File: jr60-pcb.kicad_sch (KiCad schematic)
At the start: 21 parts

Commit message: started matrix
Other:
- added sheet Matrix (matrix.kicad_sch)
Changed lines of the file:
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@@
     (pin "1")
+  )
+  (sheet (at 190.5 137.16) (size 12.7 3.81) (fields_autoplaced)
+    (stroke (width 0.1524) (type solid) (color 0 0 0 0))
+    (fill (color 0 0 0 0.0000))
+    (property "Sheet name" "Matrix" (id 0) (at 190.5 136.4484 0)
+      (effects (font (size 1.27 1.27)) (justify left bottom))
+    )
+    (property "Sheet file" "matrix.kicad_sch" (id 1) (at 190.5 141.5546 0)
+      (effects (font (size 1.27 1.27)) (justify left top))
+    )
   )
   (sheet_instances
     (path "/" (page "1"))
+    (path "/a32c9d6a-15a8-4264-8189-26275dcc1052" (page "2"))
   )
   (symbol_instances
@@
       (reference "C?") (unit 1) (value "22pF") (footprint "")
     )
+    (path "/a32c9d6a-15a8-4264-8189-26275dcc1052/00a164fa-38f9-42b5-9176-f808ef7fc89b"
+      (reference "D?") (unit 1) (value "D") (footprint "")
+    )
+    (path "/a32c9d6a-15a8-4264-8189-26275dcc1052/1690ef0f-ed90-4e63-8703-bcf22794eefd"
+      (reference "D?") (unit 1) (value "D") (footprint "")
+    )
+    (path "/a32c9d6a-15a8-4264-8189-26275dcc1052/2055ae58-06be-409a-ba1d-226477b90fa3"
+      (reference "D?") (unit 1) (value "D") (footprint "")
+    )
+    (path "/a32c9d6a-15a8-4264-8189-26275dcc1052/256b5fc0-1704-4c45-8ea4-4429ee40f749"
+      (reference "D?") (unit 1) (value "D") (footprint "")
+    )
+    (path "/a32c9d6a-15a8-4264-8189-26275dcc1052/2daa499a-0452-4e25-a168-f52ca4e61051"
+      (reference "D?") (unit 1) (value "D") (footprint "")
+    )
+    (path "/a32c9d6a-15a8-4264-8189-26275dcc1052/4475a45f-f66b-4d46-a6b3-5d0b7a07f381"
+      (reference "D?") (unit 1) (value "D") (footprint "")
+    )
+    (path "/a32c9d6a-15a8-4264-8189-26275dcc1052/673fbb2d-67e6-4422-babd-1c722f27fe06"
+      (reference "D?") (unit 1) (value "D") (footprint "")
+    )
+    (path "/a32c9d6a-15a8-4264-8189-26275dcc1052/6aa7918a-25ec-4234-ab4e-f36b24d3656e"
+      (reference "D?") (unit 1) (value "D") (footprint "")
+    )
+    (path "/a32c9d6a-15a8-4264-8189-26275dcc1052/6fa366ad-4923-4d19-8802-676ddee5e0e0"
+      (reference "D?") (unit 1) (value "D") (footprint "")
+    )
+    (path "/a32c9d6a-15a8-4264-8189-26275dcc1052/c1094195-1728-48eb-8a50-fb01f7df6b81"
+      (reference "D?") (unit 1) (value "D") (footprint "")
+    )
+    (path "/a32c9d6a-15a8-4264-8189-26275dcc1052/daefa49c-c704-4635-9fa9-c4869461e1d4"
+      (reference "D?") (unit 1) (value "D") (footprint "")
+    )
+    (path "/a32c9d6a-15a8-4264-8189-26275dcc1052/e3ffa089-507a-4b9c-8ba1-bd98d2fa1ee4"
+      (reference "D?") (unit 1) (value "D") (footprint "")
+    )
+    (path "/a32c9d6a-15a8-4264-8189-26275dcc1052/f284845e-8cec-4b95-9641-34a7256df181"
+      (reference "D?") (unit 1) (value "D") (footprint "")
+    )
+    (path "/a32c9d6a-15a8-4264-8189-26275dcc1052/f9cbd109-bc43-4c58-8da7-c90cf3420d21"
+      (reference "D?") (unit 1) (value "D") (footprint "")
+    )
     (path "/c0d774bc-a44d-4b6a-9b9c-a6a7c3bfec6e"
       (reference "F?") (unit 1) (value "Polyfuse_Small") (footprint "")
@@
       (reference "J?") (unit 1) (value "AVR-ISP-6") (footprint "")
     )
+    (path "/a32c9d6a-15a8-4264-8189-26275dcc1052/1a1701f0-a37f-44d1-8366-4f1edb2b9779"
+      (reference "K?") (unit 1) (value "SW_Push") (footprint "")
+    )
+    (path "/a32c9d6a-15a8-4264-8189-26275dcc1052/218fdd50-8063-47dd-869e-3c66a52712ca"
+      (reference "K?") (unit 1) (value "SW_Push") (footprint "")
+    )
+    (path "/a32c9d6a-15a8-4264-8189-26275dcc1052/2a6cf2fc-09a9-4db6-82ab-be40098129f8"
+      (reference "K?") (unit 1) (value "SW_Push") (footprint "")
+    )
+    (path "/a32c9d6a-15a8-4264-8189-26275dcc1052/497bc920-a0c1-4136-9bcf-893071f951d9"
+      (reference "K?") (unit 1) (value "SW_Push") (footprint "")
+    )
+    (path "/a32c9d6a-15a8-4264-8189-26275dcc1052/68e190f2-d860-4fdd-b61c-0f7741ce89fc"
+      (reference "K?") (unit 1) (value "SW_Push") (footprint "")
+    )
+    (path "/a32c9d6a-15a8-4264-8189-26275dcc1052/79d9e2c5-69c7-4b71-8e1a-5d45705f6af0"
+      (reference "K?") (unit 1) (value "SW_Push") (footprint "")
+    )
+    (path "/a32c9d6a-15a8-4264-8189-26275dcc1052/917338b5-ee95-47c0-8555-7931f20dad58"
+      (reference "K?") (unit 1) (value "SW_Push") (footprint "")
+    )
+    (path "/a32c9d6a-15a8-4264-8189-26275dcc1052/9302bd53-ef05-46bf-8ffa-7afdd80f9350"
+      (reference "K?") (unit 1) (value "SW_Push") (footprint "")
+    )
+    (path "/a32c9d6a-15a8-4264-8189-26275dcc1052/acd53b94-623c-43fd-8dc1-2293fa782ed0"
+      (reference "K?") (unit 1) (value "SW_Push") (footprint "")
+    )
+    (path "/a32c9d6a-15a8-4264-8189-26275dcc1052/baf2d5a9-c7ab-476c-b992-2d32105450ab"
+      (reference "K?") (unit 1) (value "SW_Push") (footprint "")
+    )
+    (path "/a32c9d6a-15a8-4264-8189-26275dcc1052/bc588dd7-6cd7-4f4f-bfeb-3b9f971a05ce"
+      (reference "K?") (unit 1) (value "SW_Push") (footprint "")
+    )
+    (path "/a32c9d6a-15a8-4264-8189-26275dcc1052/bfaabf9f-8945-4329-9578-c89d395de672"
+      (reference "K?") (unit 1) (value "SW_Push") (footprint "")
+    )
+    (path "/a32c9d6a-15a8-4264-8189-26275dcc1052/c64f3bde-769f-46f9-900b-e94fb5716cdc"
+      (reference "K?") (unit 1) (value "SW_Push") (footprint "")
+    )
+    (path "/a32c9d6a-15a8-4264-8189-26275dcc1052/d4076c6d-89b3-4ef4-aebf-2b683fcda264"
+      (reference "K?") (unit 1) (value "SW_Push") (footprint "")
+    )
     (path "/0b615a32-9f1a-432f-9d20-2774406301bf"

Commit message: finished schematic
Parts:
- gave numbers to parts that had none: 21
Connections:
- net row0: now reaches U1.1 (PE6)
- net col8: now reaches U1.19 (PD1)
- net col9: now reaches U1.20 (PD2)
- net col10: now reaches U1.21 (PD3)
- net col11: now reaches U1.22 (PD5)
- net col12: now reaches U1.25 (PD4)
- net col13: now reaches U1.26 (PD6)
- net col0: now reaches U1.28 (PB4)
- net col1: now reaches U1.29 (PB5)
- net col2: now reaches U1.30 (PB6)
- net col3: now reaches U1.31 (PC6)
- net col4: now reaches U1.32 (PC7)
- net col6: now reaches U1.36 (PF7)
- net col5: now reaches U1.37 (PF6)
- net row1: now reaches U1.38 (PF5)
- net row4: now reaches U1.39 (PF4)
- net row3: now reaches U1.40 (PF1)
- net row2: now reaches U1.41 (PF0)
- net col7: now reaches U1.8 (PB0)
- no-connect marks 3 -> 6

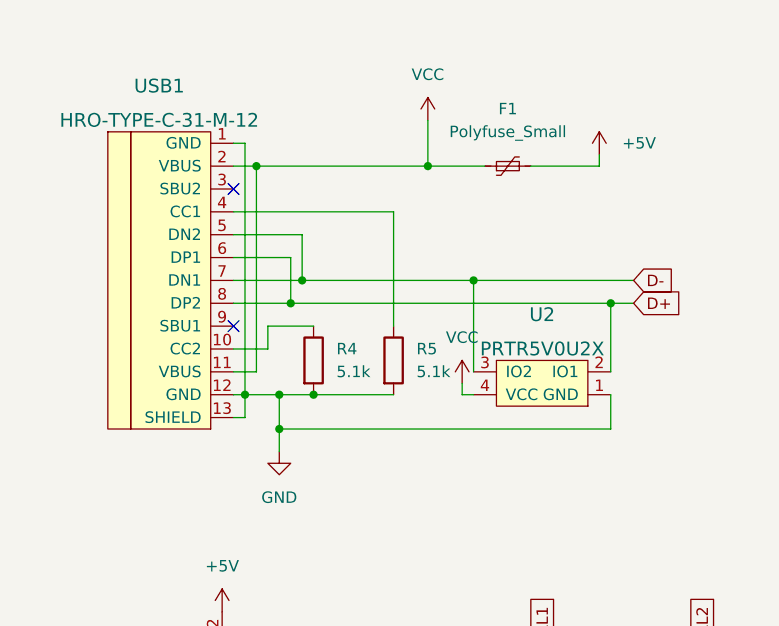
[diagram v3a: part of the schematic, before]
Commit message: added power flags
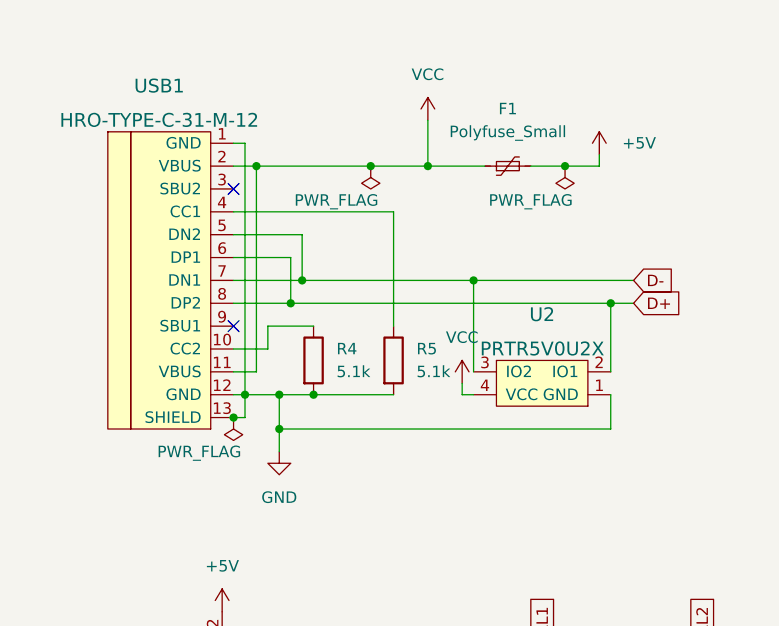
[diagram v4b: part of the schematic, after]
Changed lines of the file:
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@@
   (junction (at 195.58 49.53) (diameter 0) (color 0 0 0 0)
   )
+  (junction (at 128.27 82.55) (diameter 0) (color 0 0 0 0)
+  )
   (junction (at 129.54 53.34) (diameter 0) (color 0 0 0 0)
   )
@@
   (junction (at 175.26 49.53) (diameter 0) (color 0 0 0 0)
   )
+  (junction (at 113.03 110.49) (diameter 0) (color 0 0 0 0)
+  )
   (junction (at 185.42 54.61) (diameter 0) (color 0 0 0 0)
+  )
+  (junction (at 149.86 82.55) (diameter 0) (color 0 0 0 0)
   )
   (junction (at 195.58 54.61) (diameter 0) (color 0 0 0 0)
@@
     (stroke (width 0) (type default) (color 0 0 0 0))
   )
+  (wire (pts (xy 128.27 82.55) (xy 134.62 82.55))
+    (stroke (width 0) (type default) (color 0 0 0 0))
+  )
   (wire (pts (xy 269.24 69.85) (xy 255.27 69.85))
     (stroke (width 0) (type default) (color 0 0 0 0))
@@
     (stroke (width 0) (type default) (color 0 0 0 0))
   )
+  (wire (pts (xy 149.86 82.55) (xy 146.05 82.55))
+    (stroke (width 0) (type default) (color 0 0 0 0))
+  )
   (wire (pts (xy 156.21 151.13) (xy 161.29 151.13))
     (stroke (width 0) (type default) (color 0 0 0 0))
@@
     (stroke (width 0) (type default) (color 0 0 0 0))
   )
-  (wire (pts (xy 153.67 82.55) (xy 146.05 82.55))
+  (wire (pts (xy 153.67 82.55) (xy 149.86 82.55))
     (stroke (width 0) (type default) (color 0 0 0 0))
   )
@@
     (stroke (width 0) (type default) (color 0 0 0 0))
   )
-  (wire (pts (xy 115.57 82.55) (xy 134.62 82.55))
+  (wire (pts (xy 115.57 82.55) (xy 128.27 82.55))
     (stroke (width 0) (type default) (color 0 0 0 0))
   )
@@
     (pin "2")
   )
+  (symbol (lib_id "power:PWR_FLAG") (at 149.86 82.55 0) (mirror x) (unit 1)
+    (in_bom yes) (on_board yes)
+    (property "Reference" "#FLG0102" (id 0) (at 149.86 84.455 0)
+      (effects (font (size 1.27 1.27)) hide)
+    )
+    (property "Value" "PWR_FLAG" (id 1) (at 146.05 86.36 0))
+    (property "Footprint" "" (id 2) (at 149.86 82.55 0)
+      (effects (font (size 1.27 1.27)) hide)
+    )
+    (property "Datasheet" "~" (id 3) (at 149.86 82.55 0)
+      (effects (font (size 1.27 1.27)) hide)
+    )
+    (pin "1")
+  )
   (symbol (lib_id "power:+5V") (at 129.54 39.37 0) (unit 1)
     (in_bom yes) (on_board yes) (fields_autoplaced)
@@
     )
     (property "Datasheet" "" (id 3) (at 185.42 58.42 0)
+      (effects (font (size 1.27 1.27)) hide)
+    )
+    (pin "1")
+  )
+  (symbol (lib_id "power:PWR_FLAG") (at 128.27 82.55 0) (mirror x) (unit 1)
+    (in_bom yes) (on_board yes)
+    (property "Reference" "#FLG0101" (id 0) (at 128.27 84.455 0)
+      (effects (font (size 1.27 1.27)) hide)
+    )
+    (property "Value" "PWR_FLAG" (id 1) (at 124.46 86.36 0))
+    (property "Footprint" "" (id 2) (at 128.27 82.55 0)
+      (effects (font (size 1.27 1.27)) hide)
+    )
+    (property "Datasheet" "~" (id 3) (at 128.27 82.55 0)
       (effects (font (size 1.27 1.27)) hide)
     )
@@
     )
     (property "Datasheet" "" (id 3) (at 138.43 106.68 0)
+      (effects (font (size 1.27 1.27)) hide)
+    )
+    (pin "1")
+  )
+  (symbol (lib_id "power:PWR_FLAG") (at 113.03 110.49 0) (mirror x) (unit 1)
+    (in_bom yes) (on_board yes)
+    (property "Reference" "#FLG0103" (id 0) (at 113.03 112.395 0)
+      (effects (font (size 1.27 1.27)) hide)
+    )
+    (property "Value" "PWR_FLAG" (id 1) (at 109.22 114.3 0))
+    (property "Footprint" "" (id 2) (at 113.03 110.49 0)
+      (effects (font (size 1.27 1.27)) hide)
+    )
+    (property "Datasheet" "~" (id 3) (at 113.03 110.49 0)
       (effects (font (size 1.27 1.27)) hide)
     )
@@
   )
   (symbol_instances
+    (path "/5519e27d-ed94-4fc9-8e77-8f0d1e02ee3d"
+      (reference "#FLG0101") (unit 1) (value "PWR_FLAG") (footprint "")
+    )
+    (path "/0cfec389-6b73-4526-b5a9-72df05e052d3"
+      (reference "#FLG0102") (unit 1) (value "PWR_FLAG") (footprint "")
+    )
+    (path "/e3c81438-fb8d-4106-9e8f-d710c372b033"
+      (reference "#FLG0103") (unit 1) (value "PWR_FLAG") (footprint "")
+    )
     (path "/16adff72-6aad-4163-9f91-24e36ab48c37"
       (reference "#PWR01") (unit 1) (value "+5V") (footprint "")

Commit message: added footprints
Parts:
- C1, C2, C3, C4, C5, C6, C7, C8: footprint (none) -> Capacitor_SMD:C_0805_2012Metric_Pad1.18x1.45mm_HandSolder
- F1: footprint (none) -> Fuse:Fuse_1206_3216Metric_Pad1.42x1.75mm_HandSolder
- J1: footprint (none) -> random-keyboard-parts:Reset_Pretty-Mask
- R1, R2, R3, R4, R5, R6: footprint (none) -> Resistor_SMD:R_0805_2012Metric_Pad1.20x1.40mm_HandSolder
- SW1: footprint (none) -> Button_Switch_SMD:SW_SPST_SKQG_WithStem
- U2: footprint (none) -> random-keyboard-parts:SOT143B
- USB1: footprint (none) -> Type-C:HRO-TYPE-C-31-M-12-HandSoldering
- X1: footprint (none) -> Crystal:Crystal_SMD_3225-4Pin_3.2x2.5mm_HandSoldering

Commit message: created pcb w/o traces
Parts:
- SW1: footprint Button_Switch_SMD:SW_SPST_SKQG_WithStem -> Button_Switch_SMD:SW_SPST_TL3342
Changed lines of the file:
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@@
     (property "Reference" "SW1" (id 0) (at 119.38 45.72 0))
     (property "Value" "SW_Push" (id 1) (at 119.38 48.26 0))
-    (property "Footprint" "Button_Switch_SMD:SW_SPST_SKQG_WithStem" (id 2) (at 119.38 48.26 0)
+    (property "Footprint" "Button_Switch_SMD:SW_SPST_TL3342" (id 2) (at 119.38 48.26 0)
       (effects (font (size 1.27 1.27)) hide)
     )
@@
     )
     (path "/a32c9d6a-15a8-4264-8189-26275dcc1052/4bf5ad76-f340-4001-9ab7-d9f04a485fe6"
-      (reference "K41") (unit 1) (value "\\|") (footprint "MX_Alps_Hybrid:MX-1U")
+      (reference "K41") (unit 1) (value "DEL") (footprint "MX_Alps_Hybrid:MX-1U")
     )
     (path "/a32c9d6a-15a8-4264-8189-26275dcc1052/cdcadf60-edb9-4b66-821d-83ca054d55f9"
@@
     )
     (path "/a32c9d6a-15a8-4264-8189-26275dcc1052/740f7fe6-f69f-4959-844a-f5f794797de6"
-      (reference "K59") (unit 1) (value "SPACE") (footprint "MX_Alps_Hybrid:MX-7U")
+      (reference "K59") (unit 1) (value "SPACE") (footprint "MX_Alps_Hybrid:MX-7U-ReversedStabilizers")
     )
     (path "/a32c9d6a-15a8-4264-8189-26275dcc1052/72ab3c4c-d869-4624-af2c-544b3736c941"
@@
     )
     (path "/c4dccd53-56f1-405c-a7d8-0da9d2216803"
-      (reference "SW1") (unit 1) (value "SW_Push") (footprint "Button_Switch_SMD:SW_SPST_SKQG_WithStem")
+      (reference "SW1") (unit 1) (value "SW_Push") (footprint "Button_Switch_SMD:SW_SPST_TL3342")
     )
     (path "/f8fc9a15-9e82-47fc-b9f4-2bd9c89510e9"
